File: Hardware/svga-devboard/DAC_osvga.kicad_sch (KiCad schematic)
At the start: 27 parts, among them U1 LT1819C, U6 LT1819C

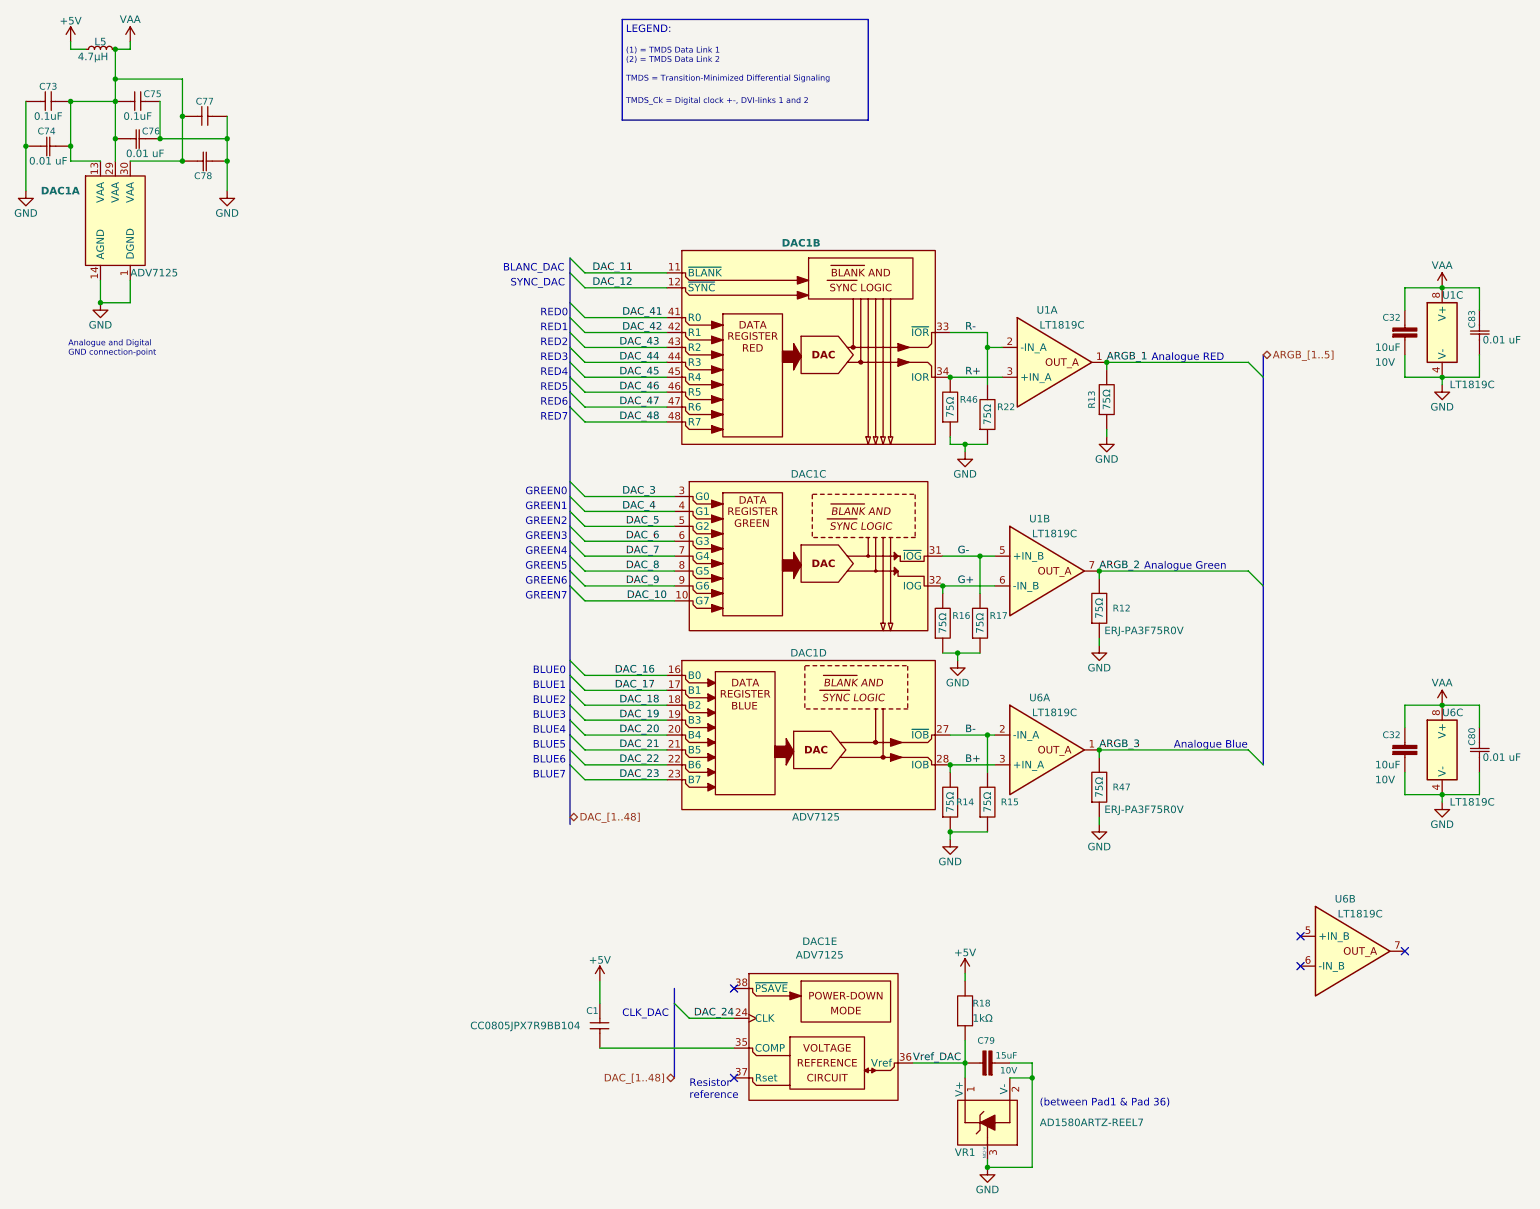
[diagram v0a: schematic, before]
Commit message: Disconnected the DVI-connectors from each other, so that they do go over the intended flat-cable to the daughter-board instead.
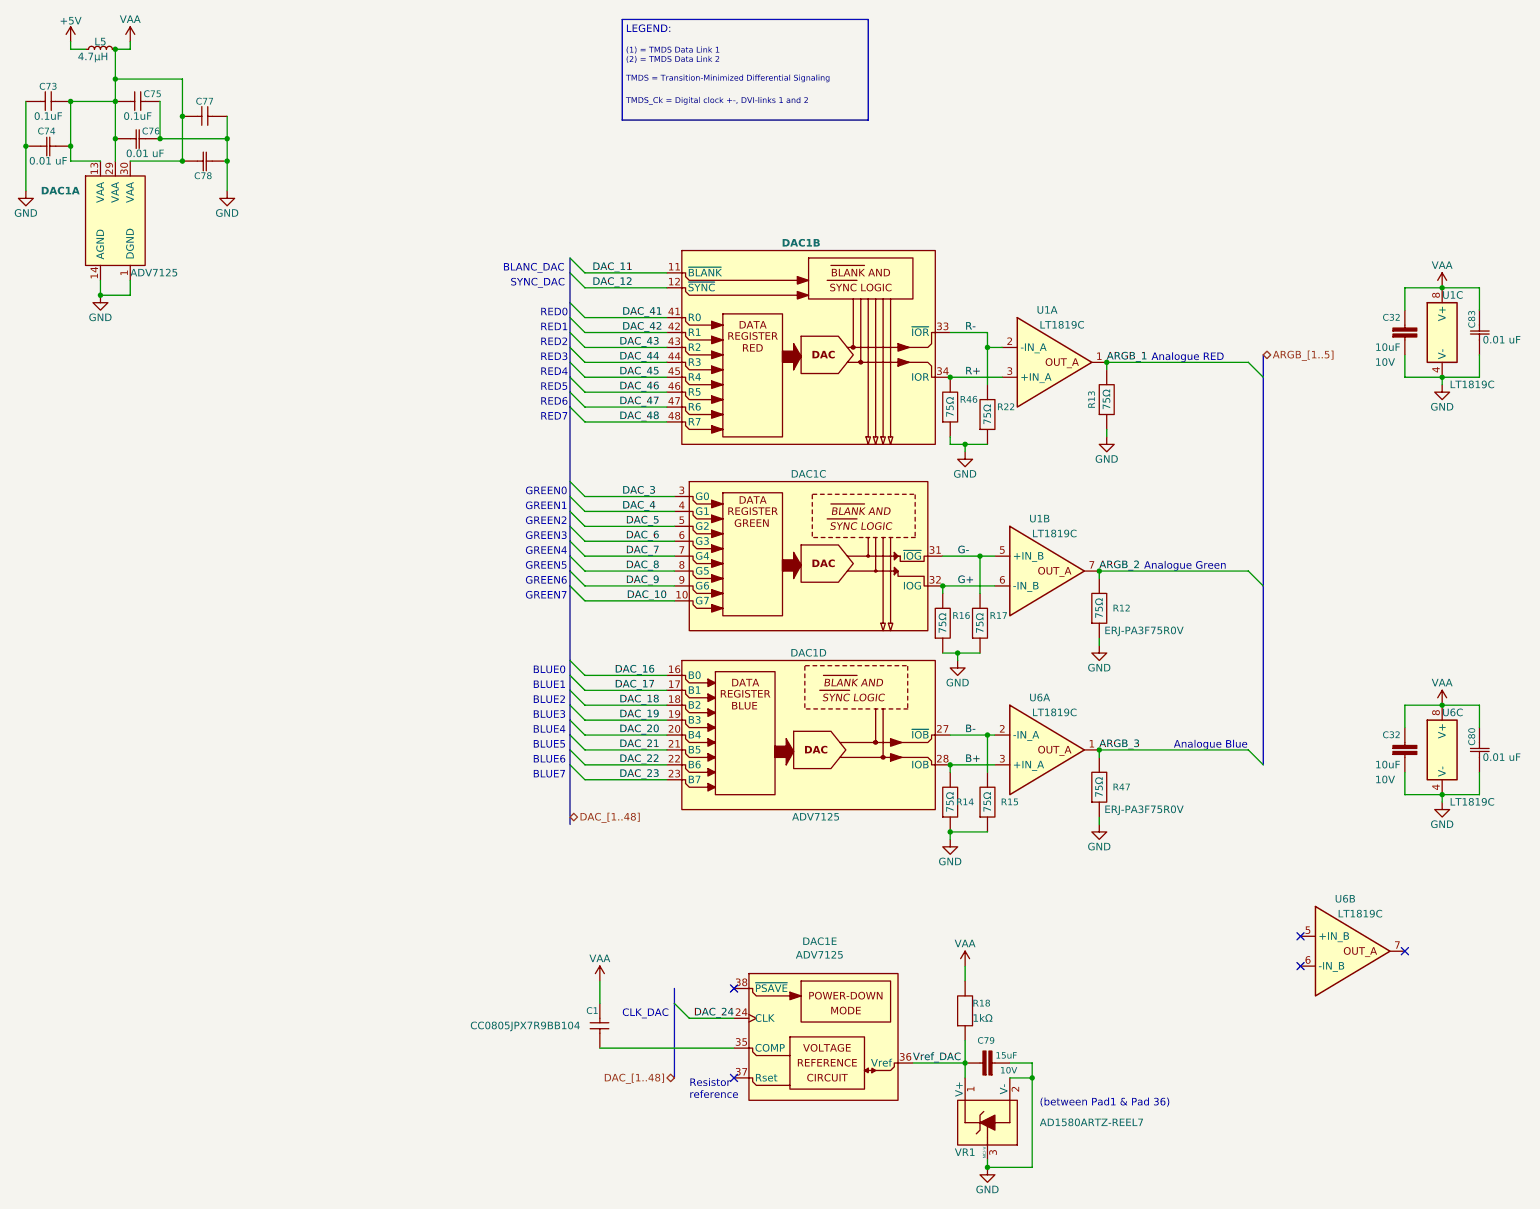
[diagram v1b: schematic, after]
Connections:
- net +5V: no longer C1.1, R18.2
- net VAA: now also C1.1, R18.2
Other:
- note removed: "Analogue and Digital GND connection-point"
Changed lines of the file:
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@@
   (junction (at 196.85 128.27) (diameter 0) (color 0 0 0 0)
   )
+  (junction (at 50.8 67.31) (diameter 0) (color 0 0 0 0)
+  )
   (junction (at 45.72 34.29) (diameter 0) (color 0 0 0 0)
   )
@@
   )
   (junction (at 201.93 142.24) (diameter 0) (color 0 0 0 0)
-  )
-  (junction (at 50.8 68.58) (diameter 0) (color 0 0 0 0)
   )
   (junction (at 279.4 137.16) (diameter 0) (color 0 0 0 0)
@@
     (stroke (width 0) (type default))
   )
-  (wire (pts (xy 50.8 64.77) (xy 50.8 68.58))
+  (wire (pts (xy 50.8 64.77) (xy 50.8 67.31))
     (stroke (width 0) (type default))
   )
@@
     (stroke (width 0) (type default))
   )
-  (wire (pts (xy 198.12 182.88) (xy 198.12 184.15))
+  (wire (pts (xy 198.12 181.61) (xy 198.12 184.15))
     (stroke (width 0) (type default))
   )
@@
     (stroke (width 0) (type default))
   )
-  (wire (pts (xy 50.8 68.58) (xy 55.88 68.58))
+  (wire (pts (xy 50.8 67.31) (xy 55.88 67.31))
     (stroke (width 0) (type default))
   )
@@
     (stroke (width 0) (type default))
   )
-  (wire (pts (xy 55.88 64.77) (xy 55.88 68.58))
+  (wire (pts (xy 55.88 64.77) (xy 55.88 67.31))
     (stroke (width 0) (type default))
   )
@@
   (text "BLUE7" (at 124.46 149.86 0)
     (effects (font (size 1.27 1.27)) (justify left bottom))
-  )
-  (text "Analogue and Digital \nGND connection-point" (at 45.3136 77.8002 0)
-    (effects (font (size 0.9906 0.9906)) (justify left bottom))
   )
   (text "Analogue RED" (at 229.87 78.74 0)
@@
     )
   )
-  (symbol (lib_id "power:+5V") (at 198.12 182.88 0) (unit 1)
-    (in_bom yes) (on_board yes) (dnp no)
-    (property "Reference" "#PWR067" (at 198.12 186.69 0)
-      (effects (font (size 1.27 1.27)) hide)
-    )
-    (property "Value" "+5V" (at 198.12 179.324 0)
-      (effects (font (size 1.27 1.27)))
-    )
-    (property "Footprint" "" (at 198.12 182.88 0)
-      (effects (font (size 1.27 1.27)) hide)
-    )
-    (property "Datasheet" "" (at 198.12 182.88 0)
-      (effects (font (size 1.27 1.27)) hide)
-    )
-    (pin "1")
-    (instances
-      (project "svga-devboard"
-        (path "/04b78285-4974-4fa0-8f4e-46d399f5727c/00000000-0000-0000-0000-000060796dc8"
-          (reference "#PWR067") (unit 1)
-        )
-      )
-    )
-  )
-  (symbol (lib_id "power:+5V") (at 135.89 184.15 0) (unit 1)
-    (in_bom yes) (on_board yes) (dnp no)
-    (property "Reference" "#PWR062" (at 135.89 187.96 0)
-      (effects (font (size 1.27 1.27)) hide)
-    )
-    (property "Value" "+5V" (at 135.89 180.594 0)
-      (effects (font (size 1.27 1.27)))
-    )
-    (property "Footprint" "" (at 135.89 184.15 0)
-      (effects (font (size 1.27 1.27)) hide)
-    )
-    (property "Datasheet" "" (at 135.89 184.15 0)
-      (effects (font (size 1.27 1.27)) hide)
-    )
-    (pin "1")
-    (instances
-      (project "svga-devboard"
-        (path "/04b78285-4974-4fa0-8f4e-46d399f5727c/00000000-0000-0000-0000-000060796dc8"
-          (reference "#PWR062") (unit 1)
-        )
-      )
-    )
-  )
   (symbol (lib_id "power:GND") (at 201.93 215.9 0) (unit 1)
     (in_bom yes) (on_board yes) (dnp no)
@@
     )
   )
-  (symbol (lib_id "power:GND") (at 50.8 68.58 0) (unit 1)
-    (in_bom yes) (on_board yes) (dnp no)
-    (property "Reference" "#PWR066" (at 50.8 74.93 0)
-      (effects (font (size 1.27 1.27)) hide)
-    )
-    (property "Value" "GND" (at 50.8 72.39 0)
-      (effects (font (size 1.27 1.27)))
-    )
-    (property "Footprint" "" (at 50.8 68.58 0)
-      (effects (font (size 1.27 1.27)) hide)
-    )
-    (property "Datasheet" "" (at 50.8 68.58 0)
+  (symbol (lib_id "power:GND") (at 50.8 67.31 0) (unit 1)
+    (in_bom yes) (on_board yes) (dnp no)
+    (property "Reference" "#PWR066" (at 50.8 73.66 0)
+      (effects (font (size 1.27 1.27)) hide)
+    )
+    (property "Value" "GND" (at 50.8 71.12 0)
+      (effects (font (size 1.27 1.27)))
+    )
+    (property "Footprint" "" (at 50.8 67.31 0)
+      (effects (font (size 1.27 1.27)) hide)
+    )
+    (property "Datasheet" "" (at 50.8 67.31 0)
       (effects (font (size 1.27 1.27)) hide)
     )
@@
     )
   )
+  (symbol (lib_id "power:VAA") (at 198.12 181.61 0) (unit 1)
+    (in_bom yes) (on_board yes) (dnp no)
+    (property "Reference" "#PWR055" (at 198.12 185.42 0)
+      (effects (font (size 1.27 1.27)) hide)
+    )
+    (property "Value" "VAA" (at 198.12 177.8 0)
+      (effects (font (size 1.27 1.27)))
+    )
+    (property "Footprint" "" (at 198.12 181.61 0)
+      (effects (font (size 1.27 1.27)) hide)
+    )
+    (property "Datasheet" "" (at 198.12 181.61 0)
+      (effects (font (size 1.27 1.27)) hide)
+    )
+    (pin "1")
+    (instances
+      (project "svga-devboard"
+        (path "/04b78285-4974-4fa0-8f4e-46d399f5727c/00000000-0000-0000-0000-000060796dc8"
+          (reference "#PWR055") (unit 1)
+        )
+      )
+    )
+  )
   (symbol (lib_id "LRJ-parts:C_GRM21BR71A106KA73K") (at 273.05 73.66 0) (unit 1)
     (in_bom yes) (on_board yes) (dnp no)
@@
         )
       )
+    )
+  )
+  (symbol (lib_id "power:VAA") (at 135.89 184.15 0) (unit 1)
+    (in_bom yes) (on_board yes) (dnp no)
+    (property "Reference" "#PWR046" (at 135.89 187.96 0)
+      (effects (font (size 1.27 1.27)) hide)
+    )
+    (property "Value" "VAA" (at 135.89 180.34 0)
+      (effects (font (size 1.27 1.27)))
+    )
+    (property "Footprint" "" (at 135.89 184.15 0)
+      (effects (font (size 1.27 1.27)) hide)
+    )
+    (property "Datasheet" "" (at 135.89 184.15 0)
+      (effects (font (size 1.27 1.27)) hide)
+    )
+    (pin "1")
+    (instances
+      (project "svga-devboard"
+        (path "/04b78285-4974-4fa0-8f4e-46d399f5727c/00000000-0000-0000-0000-000060796dc8"
+          (reference "#PWR046") (unit 1)
+        )
+      )
